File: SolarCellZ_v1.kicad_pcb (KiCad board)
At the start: 6 copper layers, 48.4 x 48.4 mm, 63 parts, among them IC1 TSL2561, J1 XF2M-1015-1A, Q1 IRLML2803, U1 NDS8434, U2 Value

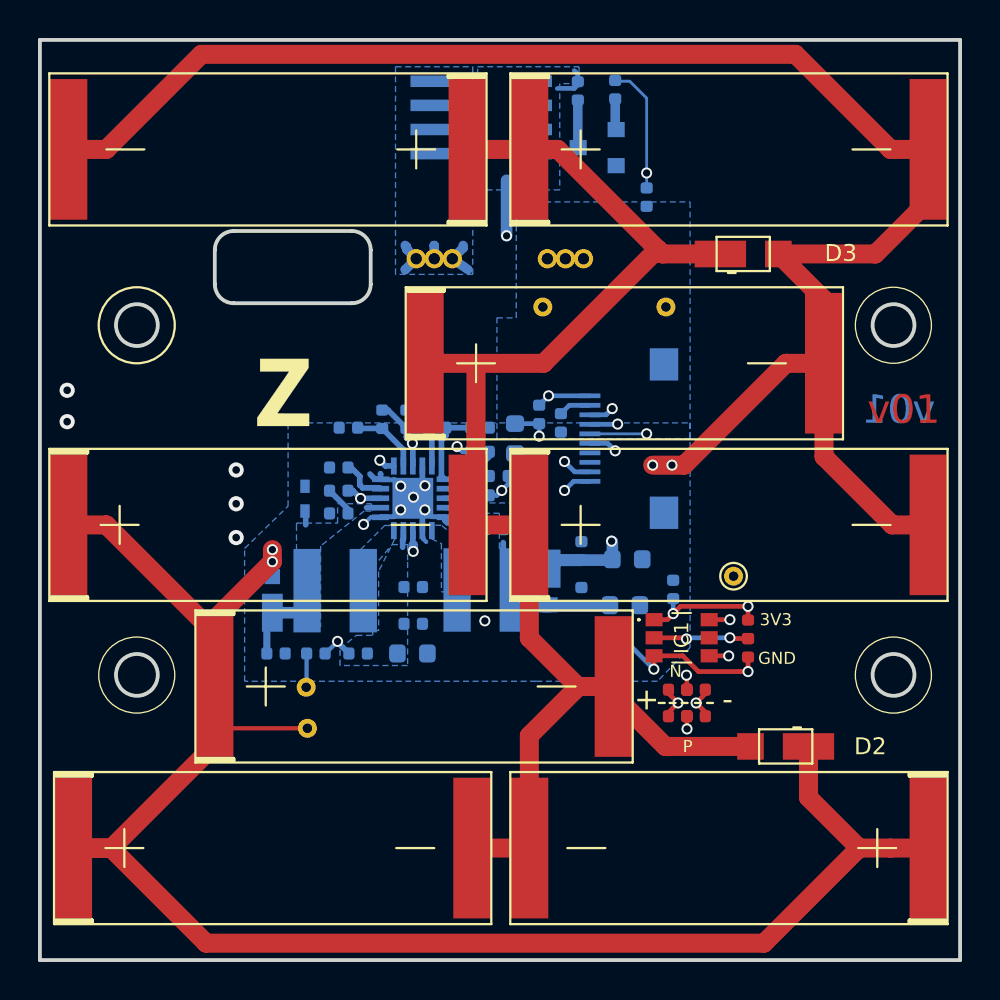
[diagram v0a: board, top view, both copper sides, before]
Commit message: fixed schematic / pcb mismatch
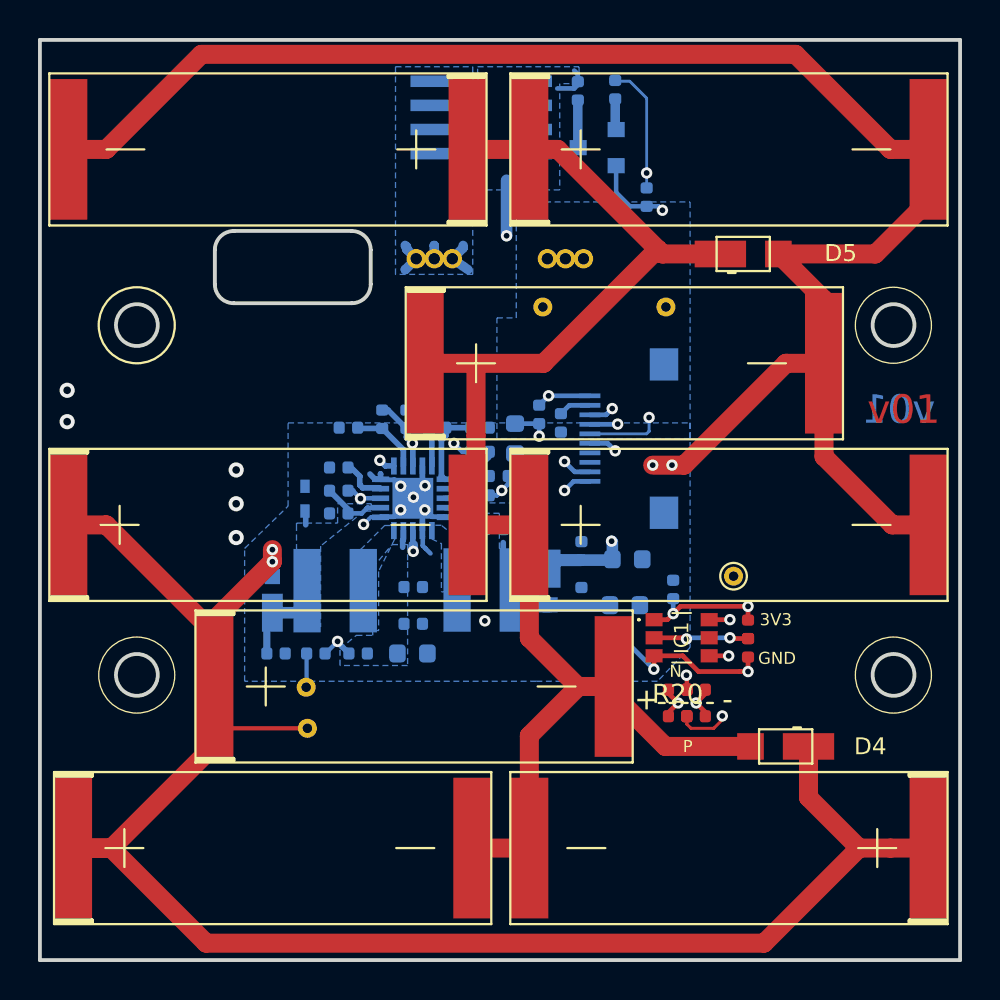
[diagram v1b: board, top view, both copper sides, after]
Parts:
- removed the D1 at (102.2, 69.5)
- removed the R2 at (123.6, 75.6)
- removed Ref**: Val**, custom-footprints:zpanel
- added D3: MSS1P4-M3_89A, misc-circuits:MICROSMP, B.Cu at (102.2, 69.5)
- added R20: 0, Resistor_SMD:R_0402_1005Metric, F.Cu at (123.5, 75.6)
- D2: footprint custom-footprints:MICROSMP -> misc-circuits:MICROSMP
- turned R2 to 0 degrees
- renumbered C1 to C5, D2 to D4, D3 to D5, R1 to R12, R2 to R13, R5 to R19, R3 to R2, R4 to R21, R19 to R22
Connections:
- IC1 pad 5: Net-(IC1-Pad5) -> (no net)
- R2 pad 1: /coil -> COIL_P
- R2 pad 2: COIL_P -> /coil
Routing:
- net GND: track 122.5 -> 127.4 mm, vias 11 -> 12
- net VSOLAR: track 6.55 -> 8.15 mm
- net Net-(C10-Pad1): track 9.20 -> 10.3 mm
- net COIL_P: track 21.0 -> 21.6 mm
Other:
- net class Default: trace_width 0.2286 -> 0.127; via_dia 0.5842 -> 0.6; via_drill 0.381 -> 0.3
- rule trace_min: 0.1524 -> 0.127
- rule via_min_size: 0.45 -> 0.6
